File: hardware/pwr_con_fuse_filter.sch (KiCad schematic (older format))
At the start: 8 parts, among them J2201 Conn_01x02, Q2201 DMP3056L, T2201 500 Ohm@100 MHz

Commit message: WIP: routing the HF Part of the Camera Connector. I have to move the clock away from the left border.
TODO: Fix DDR3 RAM.
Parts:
- added PO2101: POWER_OUTPUT, footprints:EMPTY, symbol fixme:POWER_OUTPUT
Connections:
- net labels added: +V_IN
- net labels removed: V_IN
- wire segments 24 -> 27
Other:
- note added: "TODO: maybe mor caps"
- note removed: "TODO: Footprint, maybe mor caps"
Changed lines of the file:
@@
 $Descr A4 11693 8268
 encoding utf-8
-Sheet 21 21
+Sheet 20 21
 Title ""
 Date ""
@@
 	0    1    1    0
 $EndComp
-Text HLabel 4450 2450 2    60   Output ~ 0
-V_IN
 $Comp
 L dmp3056l:DMP3056L Q2201
@@
 $EndComp
 Text Notes 6650 2950 0    60   ~ 0
-TODO: Footprint, maybe mor caps
+TODO: maybe mor caps
 Wire Wire Line
 	2500 2450 2500 2700
@@
 Connection ~ 3700 3250
 Wire Wire Line
-	4250 2450 4450 2450
+	4250 2450 4300 2450
 Wire Wire Line
 	2000 2450 1850 2450
@@
 	0    -1   -1   0
 $EndComp
+$Comp
+L power_symbols:+V_IN #PWR0193
+U 1 1 5BE964AD
+P 4400 2300
+F 0 "#PWR0193" H 4400 2150 50  0001 C CNN
+F 1 "+V_IN" H 4415 2473 50  0000 C CNN
+F 2 "" H 4400 2300 50  0001 C CNN
+F 3 "" H 4400 2300 50  0001 C CNN
+	1    4400 2300
+	1    0    0    -1
+$EndComp
+Wire Wire Line
+	4400 2450 4400 2300
+$Comp
+L fixme:POWER_OUTPUT PO2101
+U 1 1 5BEC2BFD
+P 4300 2300
+F 0 "PO2101" H 4300 2300 50  0001 C CNN
+F 1 "POWER_OUTPUT" H 4300 2450 50  0001 C CNN
+F 2 "footprints:EMPTY" H 4300 2300 50  0001 C CNN
+F 3 "" H 4300 2300 50  0001 C CNN
+	1    4300 2300
+	1    0    0    -1
+$EndComp
+Wire Wire Line
+	4300 2400 4300 2450
+Connection ~ 4300 2450
+Wire Wire Line
+	4300 2450 4400 2450
 $EndSCHEMATC

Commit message: Routed a first Version of the High Speed Part of the Camera Connector. The optional LVDS Clocks are left unconnected. I couldn't keep the Connectors Pin Assignment because it was just impossible to route.
WIP: general Routing

Fixed: DDR3 Trace Length Matching
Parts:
- removed PO2101: POWER_OUTPUT, footprints:EMPTY, symbol fixme:POWER_OUTPUT
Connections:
- wire segments 27 -> 26
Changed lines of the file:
@@
 $Descr A4 11693 8268
 encoding utf-8
-Sheet 20 21
+Sheet 19 21
 Title ""
 Date ""
@@
 Connection ~ 3700 3250
 Wire Wire Line
-	4250 2450 4300 2450
-Wire Wire Line
 	2000 2450 1850 2450
 Wire Wire Line
@@
 Wire Wire Line
 	4400 2450 4400 2300
-$Comp
-L fixme:POWER_OUTPUT PO2101
-U 1 1 5BEC2BFD
-P 4300 2300
-F 0 "PO2101" H 4300 2300 50  0001 C CNN
-F 1 "POWER_OUTPUT" H 4300 2450 50  0001 C CNN
-F 2 "footprints:EMPTY" H 4300 2300 50  0001 C CNN
-F 3 "" H 4300 2300 50  0001 C CNN
-	1    4300 2300
-	1    0    0    -1
-$EndComp
-Wire Wire Line
-	4300 2400 4300 2450
+Wire Wire Line
+	4250 2450 4300 2450
+$Comp
+L power:PWR_FLAG #FLG0112
+U 1 1 5C1ED3DC
+P 4300 2450
+F 0 "#FLG0112" H 4300 2525 50  0001 C CNN
+F 1 "PWR_FLAG" V 4250 2800 50  0000 C CNN
+F 2 "" H 4300 2450 50  0001 C CNN
+F 3 "~" H 4300 2450 50  0001 C CNN
+	1    4300 2450
+	1    0    0    -1
+$EndComp
 Connection ~ 4300 2450
 Wire Wire Line

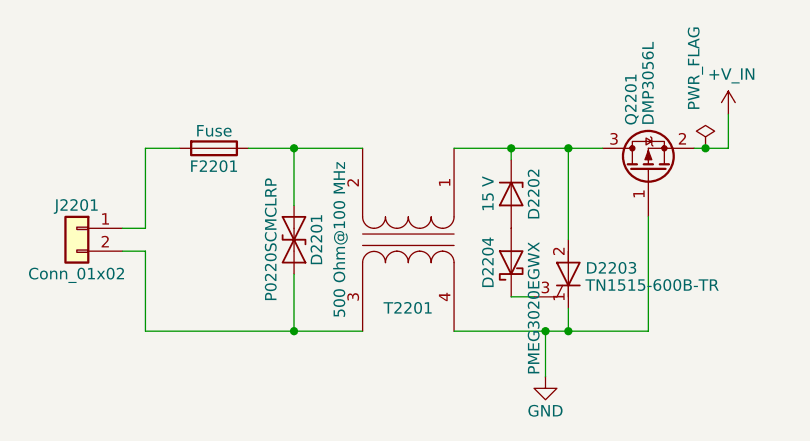
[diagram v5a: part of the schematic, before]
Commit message: Routed extra GPIO Solder Pads, reannotated the whole schematic to make it consistent.
Power Distribution routing WIP
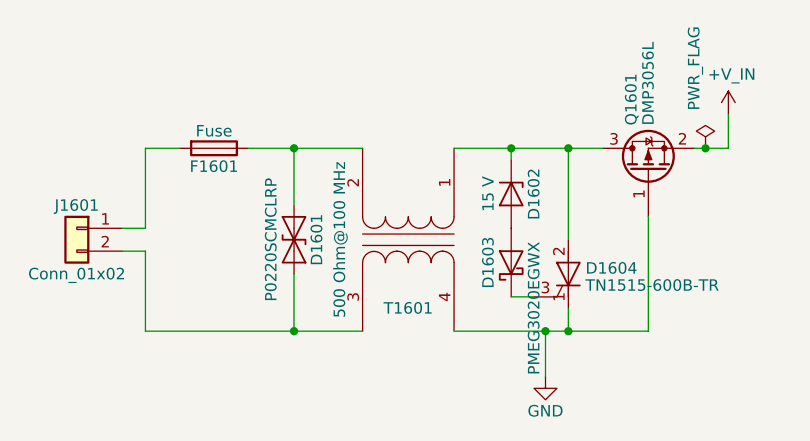
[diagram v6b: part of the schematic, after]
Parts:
- renumbered D2201 to D1601, D2202 to D1602, D2204 to D1603, D2203 to D1604, F2201 to F1601, J2201 to J1601, Q2201 to Q1601, T2201 to T1601
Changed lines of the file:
@@
 $EndDescr
 $Comp
-L Connector_Generic:Conn_01x02 J2201
+L Connector_Generic:Conn_01x02 J1601
 U 1 1 5AFB123F
 P 1550 2800
-F 0 "J2201" H 1550 2900 50  0000 C CNN
+F 0 "J1601" H 1550 2900 50  0000 C CNN
 F 1 "Conn_01x02" H 1550 2600 50  0000 C CNN
 F 2 "footprints:WAGO-890-802" H 1550 2800 50  0001 C CNN
@@
 $EndComp
 $Comp
-L Device:Transformer_1P_1S T2201
+L Device:Transformer_1P_1S T1601
 U 1 1 5AFB12DF
 P 3000 2850
-F 0 "T2201" V 3300 2850 50  0000 C CNN
+F 0 "T1601" V 3300 2850 50  0000 C CNN
 F 1 "500 Ohm@100 MHz" H 3000 2550 50  0000 C CNN
 F 2 "footprints:DLW5BTM_5.00x5.00mm" H 3000 2850 50  0001 C CNN
@@
 $EndComp
 $Comp
-L dmp3056l:DMP3056L Q2201
+L dmp3056l:DMP3056L Q1601
 U 1 1 5AFC9627
 P 4050 2550
-F 0 "Q2201" H 4250 2625 50  0000 L CNN
+F 0 "Q1601" H 4250 2625 50  0000 L CNN
 F 1 "DMP3056L" H 4250 2550 50  0000 L CNN
 F 2 "TO_SOT_Packages_SMD:SOT-23" H 4250 2475 50  0001 L CIN
@@
 $EndComp
 $Comp
-L Device:Fuse F2201
+L Device:Fuse F1601
 U 1 1 5AFC9CDC
 P 2150 2450
-F 0 "F2201" V 2230 2450 50  0000 C CNN
+F 0 "F1601" V 2230 2450 50  0000 C CNN
 F 1 "Fuse" V 2075 2450 50  0000 C CNN
 F 2 "Fuse:Fuse_1206_3216Metric" V 2080 2450 50  0001 C CNN
@@
 	3600 3250 3600 3450
 $Comp
-L Device:D_TVS D2201
+L Device:D_TVS D1601
 U 1 1 5AFCA27A
 P 2500 2850
-F 0 "D2201" H 2500 2950 50  0000 C CNN
+F 0 "D1601" H 2500 2950 50  0000 C CNN
 F 1 "P0220SCMCLRP" H 2500 2750 50  0000 C CNN
 F 2 "footprints:DO-214AA" H 2500 2850 50  0001 C CNN
@@
 Connection ~ 3600 3250
 $Comp
-L power:GND #PWR0263
+L power:GND #PWR01601
 U 1 1 5AFCA36D
 P 3600 3450
-F 0 "#PWR0263" H 3600 3200 50  0001 C CNN
+F 0 "#PWR01601" H 3600 3200 50  0001 C CNN
 F 1 "GND" H 3600 3300 50  0000 C CNN
 F 2 "" H 3600 3450 50  0001 C CNN
@@
 Connection ~ 2500 3250
 $Comp
-L Device:Q_SCR_KAG D2203
+L Device:Q_SCR_KAG D1604
 U 1 1 5B01386E
 P 3700 3000
-F 0 "D2203" H 3775 3025 50  0000 L CNN
+F 0 "D1604" H 3775 3025 50  0000 L CNN
 F 1 "TN1515-600B-TR" H 3775 2950 50  0000 L CNN
 F 2 "TO_SOT_Packages_SMD:TO-252-2" V 3700 3000 50  0001 C CNN
@@
 	3700 3250 3700 3150
 $Comp
-L Device:D_Zener D2202
+L Device:D_Zener D1602
 U 1 1 5B01397F
 P 3450 2650
-F 0 "D2202" H 3450 2750 50  0000 C CNN
+F 0 "D1602" H 3450 2750 50  0000 C CNN
 F 1 "15 V" H 3450 2550 50  0000 C CNN
 F 2 "Diodes_SMD:D_SOD-123" H 3450 2650 50  0001 C CNN
@@
 	3700 3250 4050 3250
 $Comp
-L Device:D_Schottky D2204
+L Device:D_Schottky D1603
 U 1 1 5B1B8794
 P 3450 2950
-F 0 "D2204" H 3450 3050 50  0000 C CNN
+F 0 "D1603" H 3450 3050 50  0000 C CNN
 F 1 "PMEG3020EGWX" H 3250 2850 50  0000 C CNN
 F 2 "Diodes_SMD:D_SOD-123" H 3450 2950 50  0001 C CNN
@@
 $EndComp
 $Comp
-L power_symbols:+V_IN #PWR0193
+L power_symbols:+V_IN #PWR01602
 U 1 1 5BE964AD
 P 4400 2300
-F 0 "#PWR0193" H 4400 2150 50  0001 C CNN
+F 0 "#PWR01602" H 4400 2150 50  0001 C CNN
 F 1 "+V_IN" H 4415 2473 50  0000 C CNN
 F 2 "" H 4400 2300 50  0001 C CNN
@@
 	4250 2450 4300 2450
 $Comp
-L power:PWR_FLAG #FLG0112
+L power:PWR_FLAG #FLG01601
 U 1 1 5C1ED3DC
 P 4300 2450
-F 0 "#FLG0112" H 4300 2525 50  0001 C CNN
+F 0 "#FLG01601" H 4300 2525 50  0001 C CNN
 F 1 "PWR_FLAG" V 4250 2800 50  0000 C CNN
 F 2 "" H 4300 2450 50  0001 C CNN

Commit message: general routing mainly power distribution, fixed some footprints
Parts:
- D1602, D1603: footprint Diodes_SMD:D_SOD-123 -> Diode_SMD:D_SOD-123
- D1604: footprint TO_SOT_Packages_SMD:TO-252-2 -> Package_TO_SOT_SMD:TO-252-2
- Q1601: footprint TO_SOT_Packages_SMD:SOT-23 -> Package_TO_SOT_SMD:SOT-23
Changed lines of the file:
@@
 F 0 "Q1601" H 4250 2625 50  0000 L CNN
 F 1 "DMP3056L" H 4250 2550 50  0000 L CNN
-F 2 "TO_SOT_Packages_SMD:SOT-23" H 4250 2475 50  0001 L CIN
+F 2 "Package_TO_SOT_SMD:SOT-23" H 4250 2475 50  0001 L CIN
 F 3 "https://www.diodes.com/assets/Datasheets/DMP3056L.pdf" H 4050 2550 50  0001 L CNN
 F 4 "Diodes Incorporated" H 4050 2550 60  0001 C CNN "MFG Name"
@@
 F 0 "D1604" H 3775 3025 50  0000 L CNN
 F 1 "TN1515-600B-TR" H 3775 2950 50  0000 L CNN
-F 2 "TO_SOT_Packages_SMD:TO-252-2" V 3700 3000 50  0001 C CNN
+F 2 "Package_TO_SOT_SMD:TO-252-2" V 3700 3000 50  0001 C CNN
 F 3 "http://www.st.com/content/ccc/resource/technical/document/datasheet/14/b4/09/ab/1a/e3/49/f7/CD00099707.pdf/files/CD00099707.pdf/jcr:content/translations/en.CD00099707.pdf" V 3700 3000 50  0001 C CNN
 F 4 "STMicroelectronics" H 3700 3000 60  0001 C CNN "MFG Name"
@@
 F 0 "D1602" H 3450 2750 50  0000 C CNN
 F 1 "15 V" H 3450 2550 50  0000 C CNN
-F 2 "Diodes_SMD:D_SOD-123" H 3450 2650 50  0001 C CNN
+F 2 "Diode_SMD:D_SOD-123" H 3450 2650 50  0001 C CNN
 F 3 "https://www.diodes.com/assets/Datasheets/ds18004.pdf" H 3450 2650 50  0001 C CNN
 F 4 "Diodes Incorporated" H 3450 2650 60  0001 C CNN "MFG Name"
@@
 F 0 "D1603" H 3450 3050 50  0000 C CNN
 F 1 "PMEG3020EGWX" H 3250 2850 50  0000 C CNN
-F 2 "Diodes_SMD:D_SOD-123" H 3450 2950 50  0001 C CNN
+F 2 "Diode_SMD:D_SOD-123" H 3450 2950 50  0001 C CNN
 F 3 "https://assets.nexperia.com/documents/data-sheet/PMEG3020EGW.pdf" H 3450 2950 50  0001 C CNN
 F 4 "Nexperia USA Inc." H 3450 2950 50  0001 C CNN "MFG Name"

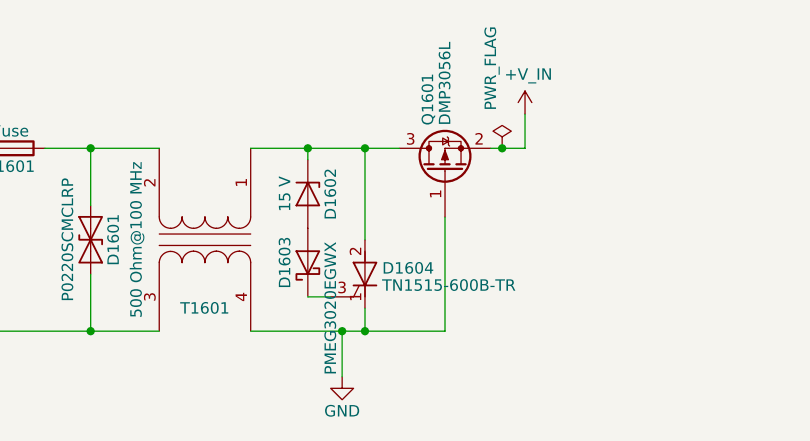
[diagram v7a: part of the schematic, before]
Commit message: First Version without any Net not routed.
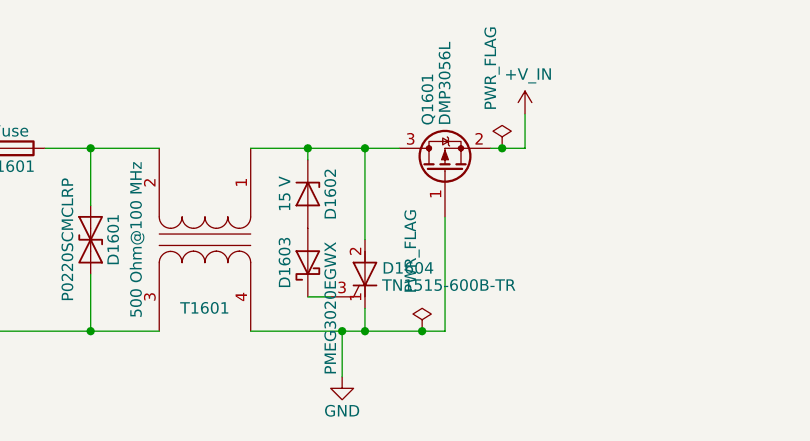
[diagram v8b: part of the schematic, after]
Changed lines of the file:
@@
 $Descr A4 11693 8268
 encoding utf-8
-Sheet 17 21
+Sheet 16 21
 Title ""
 Date ""
@@
 	3700 2450 3850 2450
 Wire Wire Line
-	3700 3250 4050 3250
+	3700 3250 3950 3250
 $Comp
 L Device:D_Schottky D1603
@@
 Wire Wire Line
 	4300 2450 4400 2450
+$Comp
+L power:PWR_FLAG #FLG0101
+U 1 1 5B633333
+P 3950 3250
+F 0 "#FLG0101" H 3950 3325 50  0001 C CNN
+F 1 "PWR_FLAG" V 3900 3600 50  0000 C CNN
+F 2 "" H 3950 3250 50  0001 C CNN
+F 3 "~" H 3950 3250 50  0001 C CNN
+	1    3950 3250
+	1    0    0    -1
+$EndComp
+Connection ~ 3950 3250
+Wire Wire Line
+	3950 3250 4050 3250
 $EndSCHEMATC
